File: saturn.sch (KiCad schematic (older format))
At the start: 7 parts, among them J1 Conn_01x09, J2 Conn_01x09, J3 DB25_Male, U1 74AHCT125N, U2 74AHCT125N, U3 74AHCT125N, U4 74AHCT125N

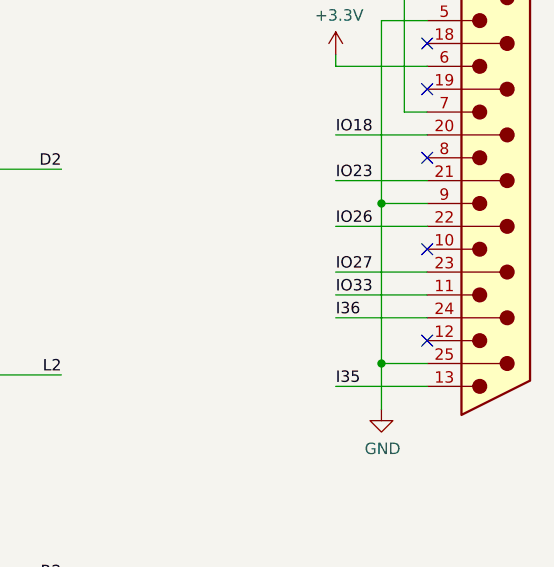
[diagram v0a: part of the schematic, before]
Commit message: Add NES schematic fixup Saturn detect pins
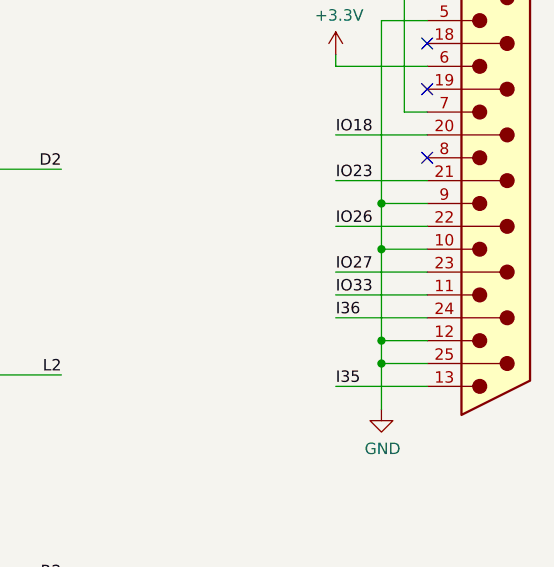
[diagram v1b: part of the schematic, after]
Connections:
- net GND: now also J3.10, J3.12
- no-connect marks 8 -> 6
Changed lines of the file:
@@
 $Descr USLetter 11000 8500
 encoding utf-8
-Sheet 2 2
+Sheet 2 3
 Title "BlueRetro - Saturn adapter cable"
 Date "2020-07-16"
@@
 Connection ~ 9150 3300
 Wire Wire Line
-	9150 3300 9150 4000
+	9150 3300 9150 3500
 Wire Wire Line
 	9350 4000 9150 4000
@@
 Wire Wire Line
 	9350 3200 8950 3200
-NoConn ~ 9350 3500
-NoConn ~ 9350 3900
 NoConn ~ 9350 2000
 NoConn ~ 9350 2600
@@
 Text Label 8950 4100 0    50   ~ 0
 I35
+Wire Wire Line
+	9350 3900 9150 3900
+Connection ~ 9150 3900
+Wire Wire Line
+	9150 3900 9150 4000
+Wire Wire Line
+	9350 3500 9150 3500
+Connection ~ 9150 3500
+Wire Wire Line
+	9150 3500 9150 3900
 $EndSCHEMATC
